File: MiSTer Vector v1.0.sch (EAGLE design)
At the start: 35 parts, among them CON2 22-23-2021, IC2 TL084, IC3 TL084, IC7 MAX6105, U1 MCP4922, U2 MCP4922, U3 MCP4922, U8 VASD1-SIP

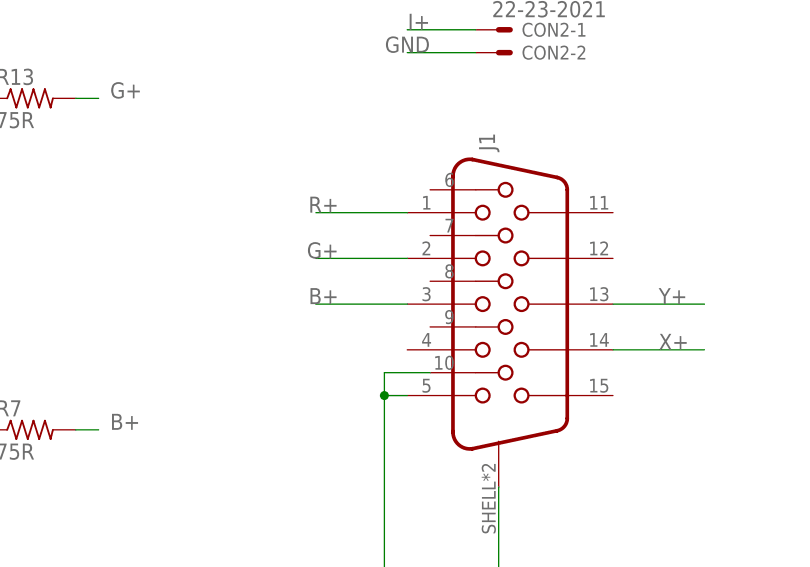
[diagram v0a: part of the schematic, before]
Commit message: hook up DE15 pins 6,7,8 to Gnd
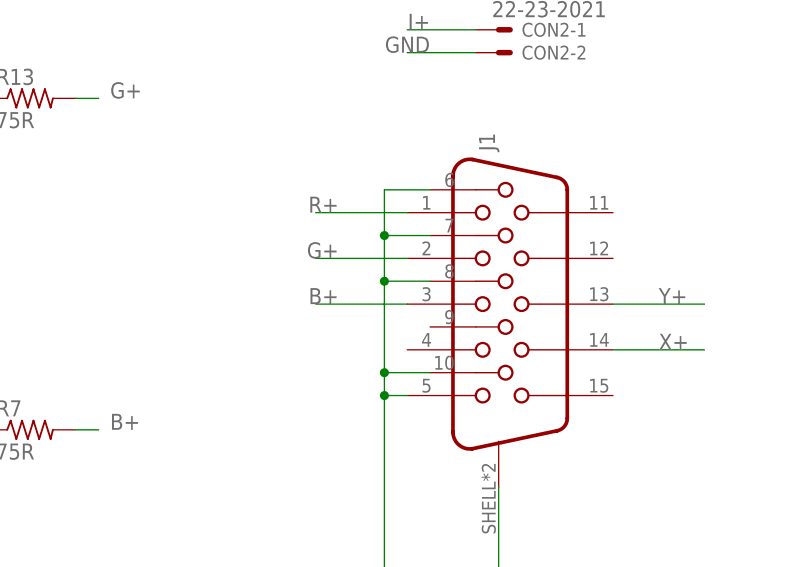
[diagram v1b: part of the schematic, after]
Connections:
- net GND: now also J1.6, J1.7, J1.8
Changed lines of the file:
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@@
 <setting verticaltext="up"/>
 </settings>
-<grid distance="0.1" unitdist="inch" unit="mil" style="lines" multiple="1" display="no" altdistance="0.01" altunitdist="inch" altunit="inch"/>
+<grid distance="0.1" unitdist="inch" unit="inch" style="lines" multiple="1" display="no" altdistance="0.01" altunitdist="inch" altunit="inch"/>
 <layers>
 <layer number="1" name="Top" color="4" fill="1" visible="no" active="no"/>
@@
 <wire x1="157.48" y1="25.4" x2="154.94" y2="25.4" width="0.1524" layer="91"/>
 <junction x="154.94" y="25.4"/>
-</segment>
-<segment>
+<pinref part="J1" gate="G$1" pin="6"/>
+<wire x1="160.02" y1="48.26" x2="154.94" y2="48.26" width="0.1524" layer="91"/>
+<wire x1="154.94" y1="48.26" x2="154.94" y2="43.18" width="0.1524" layer="91"/>
+<junction x="154.94" y="27.94"/>
+<pinref part="J1" gate="G$1" pin="7"/>
+<wire x1="154.94" y1="43.18" x2="154.94" y2="38.1" width="0.1524" layer="91"/>
+<wire x1="154.94" y1="38.1" x2="154.94" y2="27.94" width="0.1524" layer="91"/>
+<wire x1="160.02" y1="43.18" x2="154.94" y2="43.18" width="0.1524" layer="91"/>
+<junction x="154.94" y="43.18"/>
+<pinref part="J1" gate="G$1" pin="8"/>
+<wire x1="160.02" y1="38.1" x2="154.94" y2="38.1" width="0.1524" layer="91"/>
+<junction x="154.94" y="38.1"/>
+</segment>
+<segment>

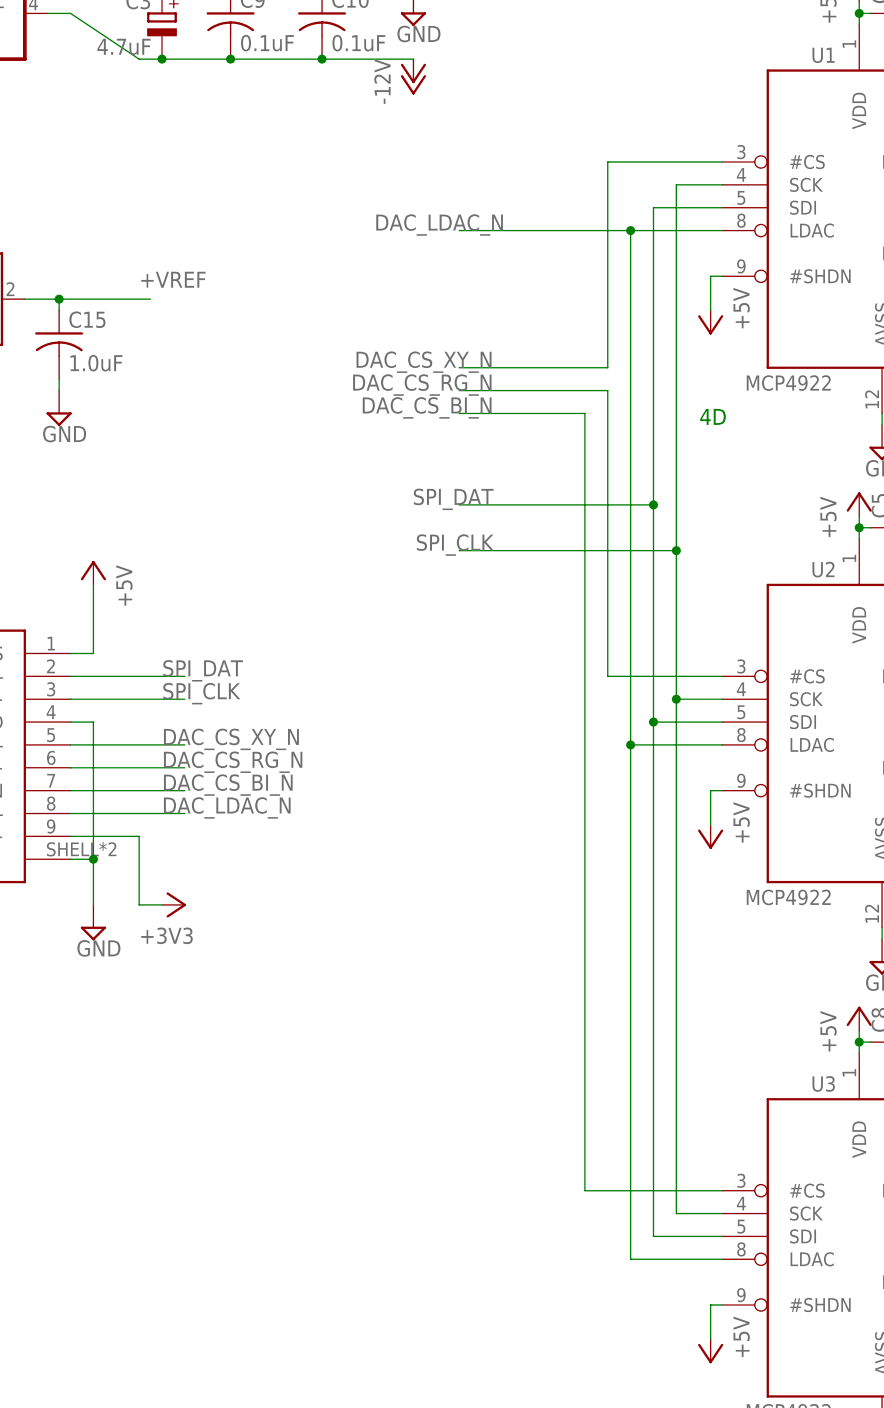
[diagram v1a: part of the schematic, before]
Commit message: driving the DAC chips in parallel now, because FPGAs rule
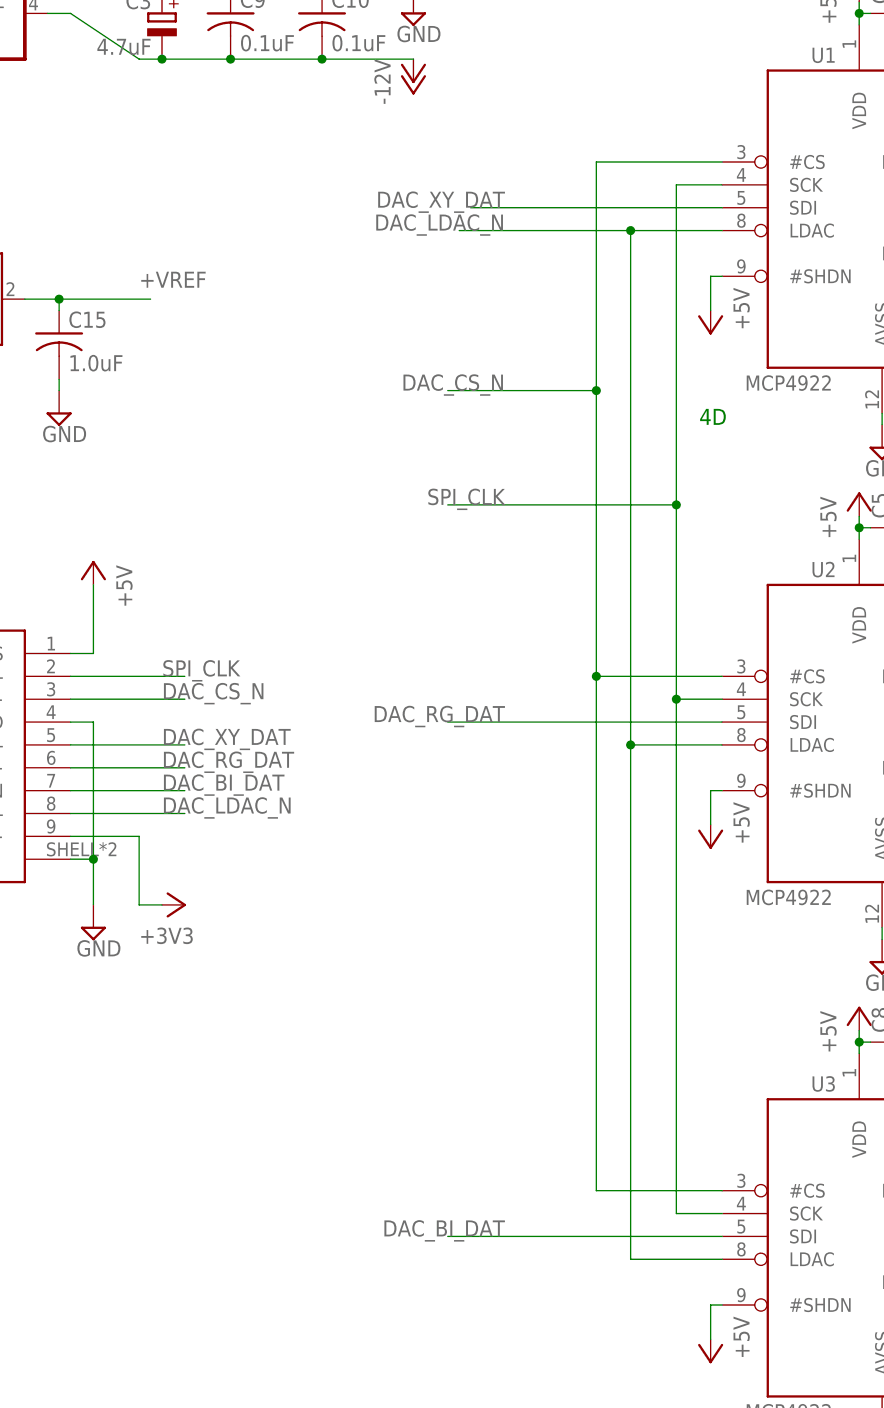
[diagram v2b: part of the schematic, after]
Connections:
- removed net DAC_CS_BI_N: U3.#CS, USBIO.GND_DRAIN
- removed net DAC_CS_RG_N: U2.#CS, USBIO.STDA_SSRX+
- removed net DAC_CS_XY_N: U1.#CS, USBIO.STDA_SSRX-
- removed net SPI_DAT: U1.SDI, U2.SDI, U3.SDI, USBIO.D-
- new net DAC_BI_DAT: U3.SDI, USBIO.GND_DRAIN
- new net DAC_CS_N: U1.#CS, U2.#CS, U3.#CS, USBIO.D+
- new net DAC_RG_DAT: U2.SDI, USBIO.STDA_SSRX+
- new net DAC_XY_DAT: U1.SDI, USBIO.STDA_SSRX-
- net SPI_CLK: now also USBIO.D-; no longer USBIO.D+
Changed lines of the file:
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@@
 <setting verticaltext="up"/>
 </settings>
-<grid distance="0.1" unitdist="inch" unit="inch" style="lines" multiple="1" display="no" altdistance="0.01" altunitdist="inch" altunit="inch"/>
+<grid distance="50" unitdist="mil" unit="mil" style="lines" multiple="1" display="no" altdistance="0.01" altunitdist="inch" altunit="inch"/>
 <layers>
 <layer number="1" name="Top" color="4" fill="1" visible="no" active="no"/>
@@
 </segment>
 </net>
-<net name="DAC_CS_RG_N" class="0">
-<segment>
-<wire x1="31.75" y1="76.2" x2="19.05" y2="76.2" width="0.1524" layer="91"/>
-<wire x1="19.05" y1="76.2" x2="19.05" y2="107.95" width="0.1524" layer="91"/>
-<wire x1="19.05" y1="107.95" x2="2.54" y2="107.95" width="0.1524" layer="91"/>
-<label x="6.35" y="107.95" size="1.778" layer="95" rot="MR0"/>
+<net name="DAC_CS_N" class="0">
+<segment>
+<wire x1="31.75" y1="76.2" x2="17.78" y2="76.2" width="0.1524" layer="91"/>
+<wire x1="17.78" y1="76.2" x2="17.78" y2="107.95" width="0.1524" layer="91"/>
+<label x="7.62" y="107.95" size="1.778" layer="95" rot="MR0"/>
 <pinref part="U2" gate="U" pin="#CS"/>
-</segment>
-<segment>
-<pinref part="USBIO" gate="G$1" pin="STDA_SSRX+"/>
-<wire x1="-40.64" y1="66.04" x2="-27.94" y2="66.04" width="0.1524" layer="91"/>
-<label x="-30.48" y="66.04" size="1.778" layer="95"/>
-</segment>
-</net>
-<net name="DAC_CS_BI_N" class="0">
-<segment>
-<wire x1="31.75" y1="19.05" x2="16.51" y2="19.05" width="0.1524" layer="91"/>
-<wire x1="2.54" y1="105.41" x2="16.51" y2="105.41" width="0.1524" layer="91"/>
-<wire x1="16.51" y1="19.05" x2="16.51" y2="105.41" width="0.1524" layer="91"/>
-<label x="6.35" y="105.41" size="1.778" layer="95" rot="MR0"/>
 <pinref part="U3" gate="U" pin="#CS"/>
-</segment>
-<segment>
-<pinref part="USBIO" gate="G$1" pin="GND_DRAIN"/>
-<wire x1="-40.64" y1="63.5" x2="-27.94" y2="63.5" width="0.1524" layer="91"/>
-<label x="-30.48" y="63.5" size="1.778" layer="95"/>
+<wire x1="17.78" y1="107.95" x2="17.78" y2="133.35" width="0.1524" layer="91"/>
+<wire x1="31.75" y1="19.05" x2="17.78" y2="19.05" width="0.1524" layer="91"/>
+<wire x1="17.78" y1="19.05" x2="17.78" y2="76.2" width="0.1524" layer="91"/>
+<junction x="17.78" y="76.2"/>
+<pinref part="U1" gate="U" pin="#CS"/>
+<wire x1="31.75" y1="133.35" x2="17.78" y2="133.35" width="0.1524" layer="91"/>
+<wire x1="17.78" y1="107.95" x2="1.27" y2="107.95" width="0.1524" layer="91"/>
+<junction x="17.78" y="107.95"/>
+</segment>
+<segment>
+<pinref part="USBIO" gate="G$1" pin="D+"/>
+<wire x1="-40.64" y1="73.66" x2="-27.94" y2="73.66" width="0.1524" layer="91"/>
+<label x="-30.48" y="73.66" size="1.778" layer="95"/>
 </segment>
 </net>
@@
 <wire x1="165.1" y1="66.04" x2="157.48" y2="66.04" width="0.1524" layer="91"/>
 <label x="160.02" y="66.04" size="1.778" layer="95" rot="MR0"/>
-</segment>
-</net>
-<net name="DAC_CS_XY_N" class="0">
-<segment>
-<wire x1="2.54" y1="110.49" x2="19.05" y2="110.49" width="0.1524" layer="91"/>
-<wire x1="19.05" y1="110.49" x2="19.05" y2="133.35" width="0.1524" layer="91"/>
-<wire x1="19.05" y1="133.35" x2="31.75" y2="133.35" width="0.1524" layer="91"/>
-<label x="6.35" y="110.49" size="1.778" layer="95" rot="MR0"/>
-<pinref part="U1" gate="U" pin="#CS"/>
-</segment>
-<segment>
-<pinref part="USBIO" gate="G$1" pin="STDA_SSRX-"/>
-<wire x1="-40.64" y1="68.58" x2="-27.94" y2="68.58" width="0.1524" layer="91"/>
-<label x="-30.48" y="68.58" size="1.778" layer="95"/>
 </segment>
 </net>
@@
 </segment>
 </net>
-<net name="SPI_DAT" class="0">
-<segment>
-<wire x1="24.13" y1="128.27" x2="31.75" y2="128.27" width="0.1524" layer="91"/>
-<wire x1="31.75" y1="71.12" x2="24.13" y2="71.12" width="0.1524" layer="91"/>
-<wire x1="24.13" y1="71.12" x2="24.13" y2="95.25" width="0.1524" layer="91"/>
-<wire x1="24.13" y1="95.25" x2="24.13" y2="128.27" width="0.1524" layer="91"/>
-<wire x1="31.75" y1="13.97" x2="24.13" y2="13.97" width="0.1524" layer="91"/>
-<wire x1="24.13" y1="13.97" x2="24.13" y2="71.12" width="0.1524" layer="91"/>
-<wire x1="2.54" y1="95.25" x2="24.13" y2="95.25" width="0.1524" layer="91"/>
-<junction x="24.13" y="71.12"/>
-<junction x="24.13" y="95.25"/>
-<label x="6.35" y="95.25" size="1.778" layer="95" rot="MR0"/>
-<pinref part="U1" gate="U" pin="SDI"/>
+<net name="DAC_RG_DAT" class="0">
+<segment>
+<wire x1="31.75" y1="71.12" x2="1.27" y2="71.12" width="0.1524" layer="91"/>
 <pinref part="U2" gate="U" pin="SDI"/>
-<pinref part="U3" gate="U" pin="SDI"/>
+<label x="7.62" y="71.12" size="1.778" layer="95" rot="MR0"/>
+</segment>
+<segment>
+<pinref part="USBIO" gate="G$1" pin="STDA_SSRX+"/>
+<wire x1="-40.64" y1="66.04" x2="-27.94" y2="66.04" width="0.1524" layer="91"/>
+<label x="-30.48" y="66.04" size="1.778" layer="95"/>
+</segment>
+</net>
+<net name="SPI_CLK" class="0">
+<segment>
+<wire x1="26.67" y1="130.81" x2="31.75" y2="130.81" width="0.1524" layer="91"/>
+<wire x1="31.75" y1="73.66" x2="26.67" y2="73.66" width="0.1524" layer="91"/>
+<wire x1="26.67" y1="73.66" x2="26.67" y2="95.25" width="0.1524" layer="91"/>
+<wire x1="26.67" y1="95.25" x2="26.67" y2="130.81" width="0.1524" layer="91"/>
+<wire x1="31.75" y1="16.51" x2="26.67" y2="16.51" width="0.1524" layer="91"/>
+<wire x1="26.67" y1="16.51" x2="26.67" y2="73.66" width="0.1524" layer="91"/>
+<wire x1="1.27" y1="95.25" x2="26.67" y2="95.25" width="0.1524" layer="91"/>
+<junction x="26.67" y="73.66"/>
+<junction x="26.67" y="95.25"/>
+<label x="7.62" y="95.25" size="1.778" layer="95" rot="MR0"/>
+<pinref part="U1" gate="U" pin="SCK"/>
+<pinref part="U2" gate="U" pin="SCK"/>
+<pinref part="U3" gate="U" pin="SCK"/>
 </segment>
 <segment>
@@
 <wire x1="-40.64" y1="76.2" x2="-27.94" y2="76.2" width="0.1524" layer="91"/>
 <label x="-30.48" y="76.2" size="1.778" layer="95"/>
-</segment>
-</net>
-<net name="SPI_CLK" class="0">
-<segment>
-<wire x1="26.67" y1="130.81" x2="31.75" y2="130.81" width="0.1524" layer="91"/>
-<wire x1="31.75" y1="73.66" x2="26.67" y2="73.66" width="0.1524" layer="91"/>
-<wire x1="26.67" y1="73.66" x2="26.67" y2="90.17" width="0.1524" layer="91"/>
-<wire x1="26.67" y1="90.17" x2="26.67" y2="130.81" width="0.1524" layer="91"/>
-<wire x1="31.75" y1="16.51" x2="26.67" y2="16.51" width="0.1524" layer="91"/>
-<wire x1="26.67" y1="16.51" x2="26.67" y2="73.66" width="0.1524" layer="91"/>
-<wire x1="2.54" y1="90.17" x2="26.67" y2="90.17" width="0.1524" layer="91"/>
-<junction x="26.67" y="73.66"/>
-<junction x="26.67" y="90.17"/>
-<label x="6.35" y="90.17" size="1.778" layer="95" rot="MR0"/>
-<pinref part="U1" gate="U" pin="SCK"/>
-<pinref part="U2" gate="U" pin="SCK"/>
-<pinref part="U3" gate="U" pin="SCK"/>
-</segment>
-<segment>
-<pinref part="USBIO" gate="G$1" pin="D+"/>
-<wire x1="-40.64" y1="73.66" x2="-27.94" y2="73.66" width="0.1524" layer="91"/>
-<label x="-30.48" y="73.66" size="1.778" layer="95"/>
 </segment>
 </net>
@@
 </segment>
 </net>
+<net name="DAC_BI_DAT" class="0">
+<segment>
+<pinref part="U3" gate="U" pin="SDI"/>
+<wire x1="31.75" y1="13.97" x2="1.27" y2="13.97" width="0.1524" layer="91"/>
+<label x="7.62" y="13.97" size="1.778" layer="95" rot="MR0"/>
+</segment>
+<segment>
+<pinref part="USBIO" gate="G$1" pin="GND_DRAIN"/>
+<wire x1="-40.64" y1="63.5" x2="-27.94" y2="63.5" width="0.1524" layer="91"/>
+<label x="-30.48" y="63.5" size="1.778" layer="95"/>
+</segment>
+</net>
+<net name="DAC_XY_DAT" class="0">
+<segment>
+<pinref part="U1" gate="U" pin="SDI"/>
+<wire x1="3.81" y1="128.27" x2="31.75" y2="128.27" width="0.1524" layer="91"/>
+<label x="7.62" y="128.27" size="1.778" layer="95" rot="MR0"/>
+</segment>
+<segment>
+<pinref part="USBIO" gate="G$1" pin="STDA_SSRX-"/>
+<wire x1="-40.64" y1="68.58" x2="-27.94" y2="68.58" width="0.1524" layer="91"/>
+<label x="-30.48" y="68.58" size="1.778" layer="95"/>
+</segment>
+</net>
